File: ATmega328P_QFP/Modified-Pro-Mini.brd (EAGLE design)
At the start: 18.3 x 33.5 mm, 19 parts, among them Q1 8/16/20MHz, U1 ATMEGA328

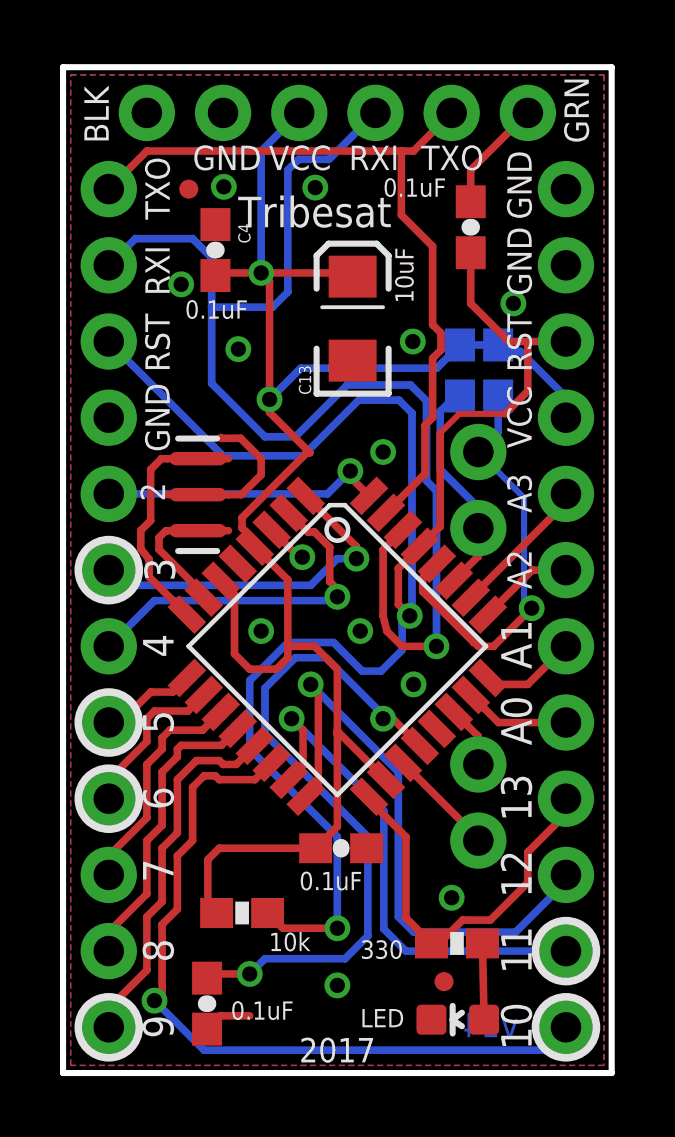
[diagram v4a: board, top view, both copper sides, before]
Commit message: Prepare silkscreen layers for OSH Park printing (#4)
* Fix typo in bPlace layer
* Remove fiducials
* Cleared the tNames layer
* Slight adjustments to prevent text from overlapping copper
* got rid of kink in TXO line
* moved via slightly
* bottom silk tweak
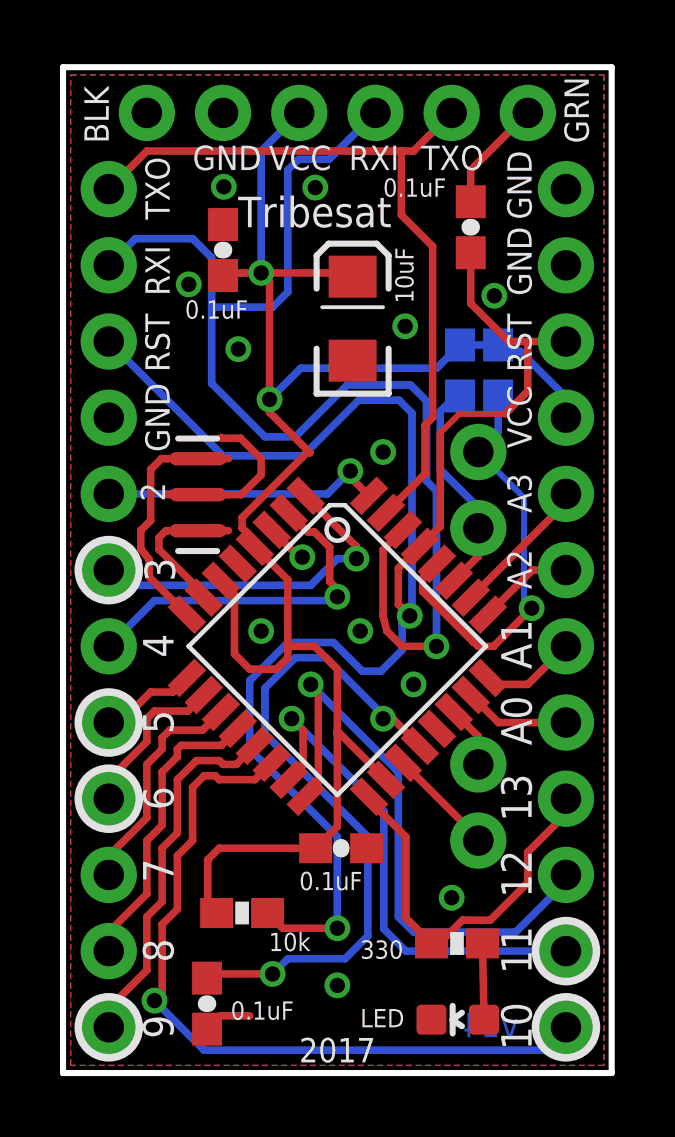
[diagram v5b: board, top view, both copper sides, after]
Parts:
- removed JP5, JP8: FIDUCIALUFIDUCIAL, SparkFun:MICRO-FIDUCIAL
- moved C4 0.25 mm to (5.08, 27.2)
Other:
- board text added: "Test Design V1.0"
- board text removed: "Test Desgine V1.0"
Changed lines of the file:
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@@
 <text x="10.414" y="28.956" size="0.6096" layer="21" font="vector" ratio="13">0.1uF</text>
 <text x="5.334" y="28.702" size="1.016" layer="22" font="vector" ratio="16" rot="MR180">Tribesat</text>
-<text x="14.224" y="24.892" size="0.8128" layer="22" font="vector" ratio="16" rot="MR0">ATmega328P QFP</text>
-<text x="9.398" y="22.86" size="0.8128" layer="22" font="vector" ratio="15" rot="MR0" align="center">Test
-Desgine
-V1.0</text>
 <text x="11.43" y="25.4" size="0.6096" layer="21" font="vector" ratio="13" rot="R90">10uF</text>
 <text x="3.81" y="24.892" size="0.6096" layer="21" font="vector" ratio="13">0.1uF</text>
+<text x="5.588" y="20.828" size="1.016" layer="22" font="vector" ratio="20" distance="10" rot="MR270">ATmega328P QFP</text>
+<text x="8.636" y="23.622" size="0.889" layer="22" font="vector" ratio="20" distance="19" rot="MR0" align="center">Test
+Design
+V1.0</text>
 </plain>
 <attributes>
@@
 <attribute name="VALUE" x="13.1064" y="22.1488" size="0.4064" layer="28" font="vector" rot="MR90"/>
 </element>
-<element name="JP5" library="SparkFun" package="MICRO-FIDUCIAL" value="FIDUCIALUFIDUCIAL" x="3.937" y="29.21"/>
-<element name="JP8" library="SparkFun" package="MICRO-FIDUCIAL" value="FIDUCIALUFIDUCIAL" x="12.446" y="2.794"/>
 <element name="JP3" library="SparkFun" package="1X02" value="" x="13.589" y="7.493" smashed="yes" rot="MR90">
 <attribute name="VALUE" x="10.414" y="6.223" size="1.27" layer="28" rot="MR90"/>
@@
 <attribute name="VALUE" x="14.478" y="26.924" size="0.4064" layer="27" font="vector" rot="R90"/>
 </element>
-<element name="C13" library="SparkFun" package="EIA3216" value="10uF" x="9.398" y="24.892" rot="R90"/>
-<element name="C4" library="SparkFun" package="0603-CAP" value="0.1uF" x="4.826" y="27.178" rot="R270"/>
+<element name="C13" library="SparkFun" package="EIA3216" value="10uF" x="9.398" y="24.892" smashed="yes" rot="R90">
+<attribute name="VALUE" x="8.066" y="25.3" size="0.4064" layer="27" rot="R90"/>
+</element>
+<element name="C4" library="SparkFun" package="0603-CAP" value="0.1uF" x="5.08" y="27.178" smashed="yes" rot="R270">
+<attribute name="VALUE" x="3.937" y="28.194" size="0.4064" layer="27" font="vector" rot="R270"/>
+</element>
 </elements>
 <signals>
@@
 <via x="10.414" y="20.447" extent="1-16" drill="0.508"/>
 <via x="6.35" y="14.478" extent="1-16" drill="0.508"/>
-<via x="14.7574" y="25.4" extent="1-16" drill="0.508"/>
+<via x="14.1224" y="25.654" extent="1-16" drill="0.508"/>
 <via x="7.7216" y="16.9418" extent="1-16" drill="0.508"/>
-<via x="3.683" y="26.035" extent="1-16" drill="0.508"/>
-<via x="11.4046" y="24.13" extent="1-16" drill="0.508"/>
+<via x="3.937" y="26.035" extent="1-16" drill="0.508"/>
+<via x="11.1506" y="24.638" extent="1-16" drill="0.508"/>
 <polygon width="0.254" layer="1" isolate="0.3048">
 <vertex x="0" y="33.02"/>
@@
 <wire x1="10.414" y1="11.557" x2="10.7372" y2="11.557" width="0.254" layer="1"/>
 <via x="10.414" y="11.557" extent="1-16" drill="0.508"/>
-<wire x1="9.144" y1="3.556" x2="6.477" y2="3.556" width="0.254" layer="16"/>
-<wire x1="6.477" y1="3.556" x2="5.969" y2="3.048" width="0.254" layer="16"/>
-<via x="5.969" y="3.048" extent="1-16" drill="0.508"/>
-<wire x1="5.969" y1="3.048" x2="4.6872" y2="3.048" width="0.254" layer="1"/>
+<wire x1="9.144" y1="3.556" x2="7.239" y2="3.556" width="0.254" layer="16"/>
+<wire x1="7.239" y1="3.556" x2="6.731" y2="3.048" width="0.254" layer="16"/>
+<via x="6.731" y="3.048" extent="1-16" drill="0.508"/>
+<wire x1="6.731" y1="3.048" x2="4.6872" y2="3.048" width="0.254" layer="1"/>
 <wire x1="4.6872" y1="3.048" x2="4.5466" y2="2.9074" width="0.254" layer="1"/>
 <wire x1="11.64248125" y1="10.651828125" x2="10.737309375" y2="11.557" width="0.254" layer="1"/>
@@
 <contactref element="JP1" pad="2"/>
 <wire x1="2.54" y1="30.48" x2="1.27" y2="29.21" width="0.254" layer="1"/>
-<wire x1="11.43" y1="30.48" x2="11.049" y2="30.48" width="0.254" layer="1"/>
+<wire x1="11.43" y1="30.48" x2="11.0236" y2="30.48" width="0.254" layer="1"/>
 <wire x1="11.0236" y1="30.48" x2="2.54" y2="30.48" width="0.254" layer="1"/>
 <wire x1="11.43" y1="30.48" x2="12.7" y2="31.75" width="0.254" layer="1"/>
-<wire x1="12.065" y1="21.59" x2="12.065" y2="23.5712" width="0.254" layer="1"/>
-<wire x1="12.065" y1="23.5712" x2="12.3444" y2="23.8506" width="0.254" layer="1"/>
-<wire x1="12.3444" y1="23.8506" x2="12.3444" y2="24.4094" width="0.254" layer="1"/>
-<wire x1="12.3444" y1="24.4094" x2="12.065" y2="24.6888" width="0.254" layer="1"/>
-<wire x1="12.065" y1="24.6888" x2="12.065" y2="27.305" width="0.254" layer="1"/>
-<wire x1="11.811" y1="21.336" x2="12.065" y2="21.59" width="0.254" layer="1"/>
+<wire x1="12.065" y1="21.59" x2="11.811" y2="21.336" width="0.254" layer="1"/>
 <wire x1="11.811" y1="19.7194" x2="11.811" y2="21.336" width="0.254" layer="1"/>
 <wire x1="10.5111125" y1="18.4195375" x2="11.810975" y2="19.7194" width="0.254" layer="1"/>
 <wire x1="11.810975" y1="19.7194" x2="11.811" y2="19.7194" width="0.254" layer="1"/>
-<wire x1="12.065" y1="27.305" x2="11.0236" y2="28.3464" width="0.254" layer="1"/>
+<wire x1="11.0236" y1="28.3464" x2="12.065" y2="27.305" width="0.254" layer="1"/>
 <wire x1="11.0236" y1="28.3464" x2="11.0236" y2="30.48" width="0.254" layer="1"/>
-<wire x1="11.0236" y1="30.48" x2="11.049" y2="30.48" width="0.254" layer="1"/>
+<wire x1="12.065" y1="27.305" x2="12.065" y2="21.59" width="0.254" layer="1"/>
 </signal>
 <signal name="VCC">
@@
 <contactref element="C13" pad="A"/>
 <contactref element="C4" pad="2"/>
-<wire x1="6.35" y1="26.416" x2="4.914" y2="26.416" width="0.254" layer="1"/>
-<wire x1="4.914" y1="26.416" x2="4.826" y2="26.328" width="0.254" layer="1"/>
+<wire x1="6.35" y1="26.416" x2="5.676" y2="26.416" width="0.254" layer="1"/>
+<wire x1="5.676" y1="26.416" x2="5.08" y2="26.328" width="0.254" layer="1"/>
 <wire x1="6.35" y1="26.416" x2="9.274" y2="26.416" width="0.254" layer="1"/>
 <wire x1="9.274" y1="26.416" x2="9.398" y2="26.292" width="0.254" layer="1"/>

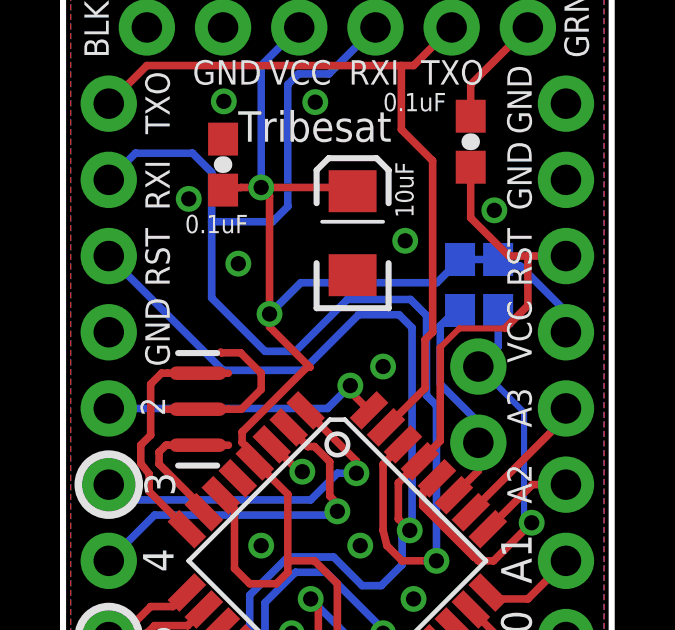
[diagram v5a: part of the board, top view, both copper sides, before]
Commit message: straigtened VCC line
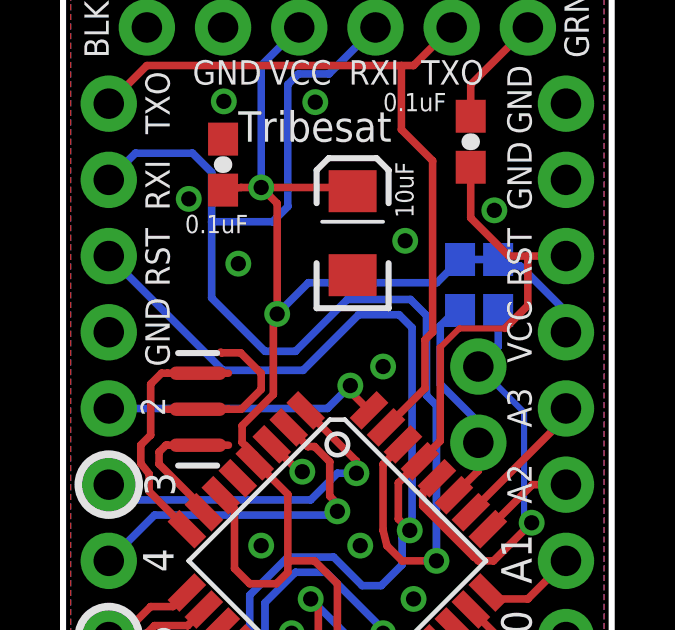
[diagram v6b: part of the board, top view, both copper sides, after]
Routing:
- net VCC: track 58.8 -> 57.7 mm
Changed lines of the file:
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@@
 <wire x1="16.51" y1="22.2758" x2="16.51" y2="21.59" width="0.254" layer="16"/>
 <wire x1="14.986" y1="23.7998" x2="16.51" y2="22.2758" width="0.254" layer="16"/>
-<wire x1="7.6708" y1="23.241" x2="12.2056" y2="23.241" width="0.254" layer="16"/>
 <wire x1="12.9794" y1="24.0148" x2="14.2494" y2="24.0148" width="0.254" layer="16"/>
-<via x="6.6294" y="22.1996" extent="1-16" drill="0.508"/>
+<via x="6.8834" y="22.1996" extent="1-16" drill="0.508"/>
 <wire x1="8.89" y1="11.0491" x2="8.89" y2="7.962" width="0.254" layer="1"/>
 <wire x1="8.89" y1="7.962" x2="8.167" y2="7.239" width="0.254" layer="1"/>
@@
 <wire x1="6.137515625" y1="17.28816875" x2="7.239" y2="16.186684375" width="0.254" layer="1"/>
 <wire x1="10.5111125" y1="9.520459375" x2="8.89" y2="11.141571875" width="0.254" layer="1"/>
-<wire x1="12.2056" y1="23.241" x2="12.9794" y2="24.0148" width="0.254" layer="16"/>
+<wire x1="12.9794" y1="24.0148" x2="12.2056" y2="23.241" width="0.254" layer="16"/>
 <wire x1="14.986" y1="23.7998" x2="14.4644" y2="23.7998" width="0.254" layer="16"/>
 <wire x1="14.4644" y1="23.7998" x2="14.2494" y2="24.0148" width="0.254" layer="16"/>
@@
 <wire x1="7.62" y1="31.75" x2="6.35" y2="30.48" width="0.254" layer="16"/>
 <wire x1="6.137515625" y1="17.313484375" x2="6.137515625" y2="17.28816875" width="0.254" layer="1"/>
-<wire x1="5.715" y1="17.9138" x2="5.715" y2="18.2626" width="0.254" layer="1"/>
-<wire x1="5.715" y1="18.2626" x2="7.874" y2="20.4216" width="0.254" layer="1"/>
 <wire x1="6.137515625" y1="17.491284375" x2="5.715" y2="17.9138" width="0.254" layer="1"/>
 <wire x1="6.137515625" y1="17.491284375" x2="6.137515625" y2="17.28816875" width="0.254" layer="1"/>
-<wire x1="7.9756" y1="20.4216" x2="6.6294" y2="21.7678" width="0.254" layer="1"/>
-<wire x1="7.6708" y1="23.241" x2="6.6294" y2="22.1996" width="0.254" layer="16"/>
-<wire x1="6.6294" y1="21.7678" x2="6.6294" y2="22.1996" width="0.254" layer="1"/>
-<wire x1="6.6294" y1="22.1996" x2="6.6294" y2="22.5044" width="0.254" layer="1"/>
 <contactref element="R2" pad="2"/>
 <wire x1="4.572" y1="6.858" x2="4.572" y2="5.373" width="0.254" layer="1"/>
 <wire x1="4.572" y1="5.373" x2="4.865" y2="5.08" width="0.254" layer="1"/>
-<wire x1="7.874" y1="20.4216" x2="7.9756" y2="20.4216" width="0.254" layer="1"/>
-<wire x1="6.6294" y1="22.1996" x2="6.6294" y2="26.1366" width="0.254" layer="1"/>
-<wire x1="6.6294" y1="26.1366" x2="6.35" y2="26.416" width="0.254" layer="1"/>
+<wire x1="6.35" y1="26.416" x2="6.6294" y2="26.1366" width="0.254" layer="1"/>
 <contactref element="C13" pad="A"/>
 <contactref element="C4" pad="2"/>
@@
 <wire x1="6.35" y1="26.416" x2="9.274" y2="26.416" width="0.254" layer="1"/>
 <wire x1="9.274" y1="26.416" x2="9.398" y2="26.292" width="0.254" layer="1"/>
+<wire x1="6.7564" y1="22.0726" x2="6.8834" y2="22.1996" width="0.254" layer="1"/>
+<wire x1="5.715" y1="18.4752625" x2="6.7564" y2="19.5166625" width="0.254" layer="1"/>
+<wire x1="6.7564" y1="19.5166625" x2="6.7564" y2="22.0726" width="0.254" layer="1"/>
+<wire x1="5.715" y1="17.9138" x2="5.715" y2="18.4752625" width="0.254" layer="1"/>
+<wire x1="6.8834" y1="22.1996" x2="6.8834" y2="25.8826" width="0.254" layer="1"/>
+<wire x1="6.8834" y1="25.8826" x2="6.35" y2="26.416" width="0.254" layer="1"/>
+<wire x1="12.2056" y1="23.241" x2="7.9248" y2="23.241" width="0.254" layer="16"/>
+<wire x1="7.9248" y1="23.241" x2="6.8834" y2="22.1996" width="0.254" layer="16"/>
 </signal>
 <signal name="D9">

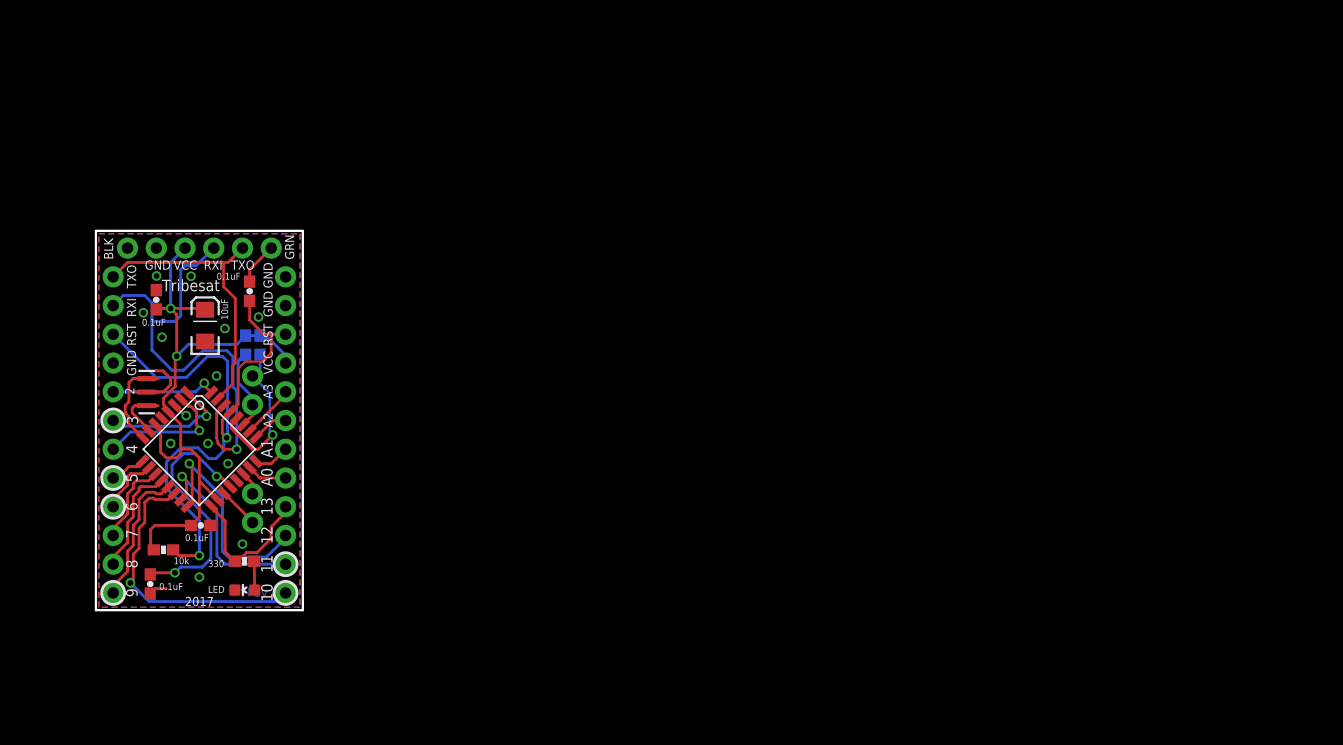
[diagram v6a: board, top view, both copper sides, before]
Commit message: New board design: - larger footprint by the ICD requirements (no holes) - removed headers - added DF12 connector footprint
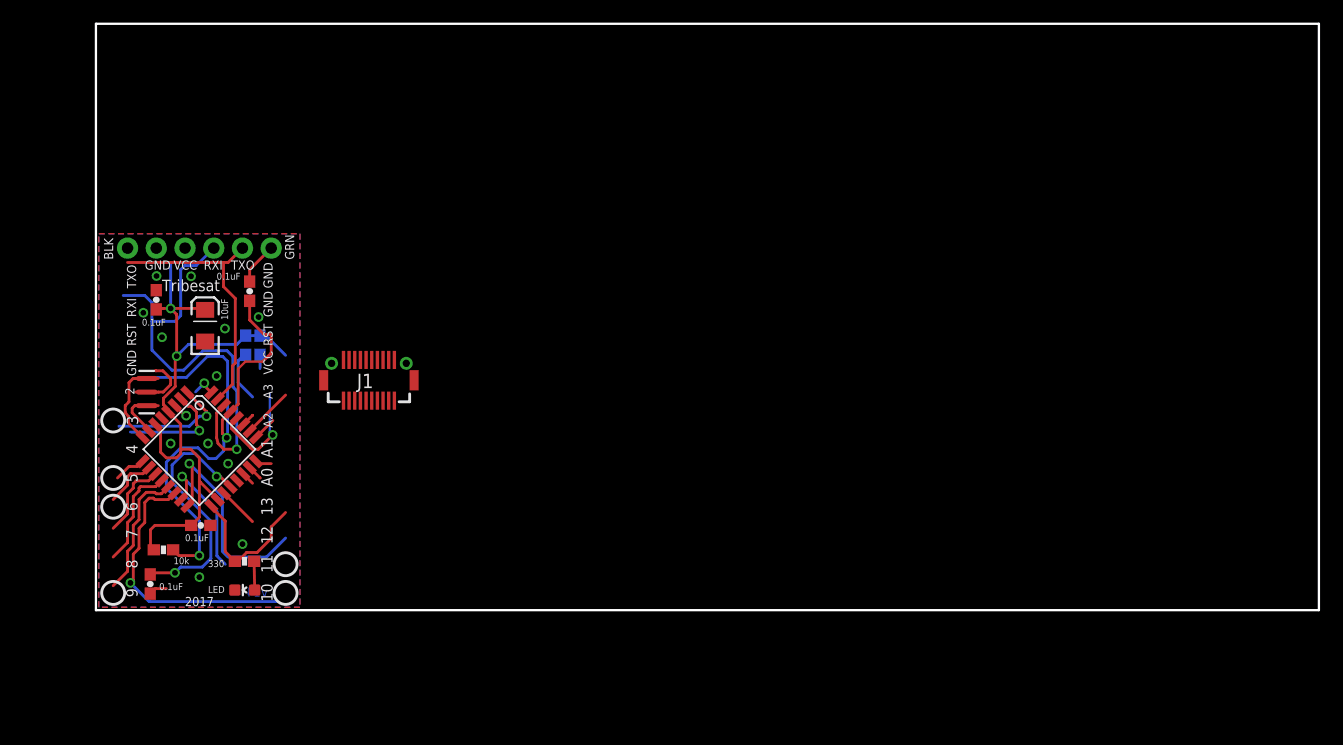
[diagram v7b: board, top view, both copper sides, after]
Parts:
- removed JP2, JP3: (no value), SparkFun:1X02
- removed JP6, JP7: (no value), SparkFun:1X12
- added J1: DF12(4.0)-20DP-0.5V(86), DF12(4.0)-20DP-0.5V(86):DF12(4.0)-20DP
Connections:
- new net 1W: J1.16
- new net 3.3V: J1.18
- new net BUSY: J1.13
- new net D1: J1.7
- new net LVRX: J1.9
- new net LVTX: J1.10
- new net N$9: J1.15
- new net NC: J1.14
- net A0: no longer JP6.8
- net A1: now also J1.1; no longer JP6.7
- net A2: now also J1.2; no longer JP6.6
- net A3: now also J1.3; no longer JP6.5
- net A4: now also J1.4; no longer JP2.1
- net A5: now also J1.5; no longer JP2.2
- net A6: now also J1.6; no longer JP3.1
- net A7: no longer JP3.2
- net D10: no longer JP6.12
- net D2: now also J1.8; no longer JP7.8
- net D3: no longer JP7.7
- net D4: no longer JP7.6
- net D5: no longer JP7.5
- net D6: no longer JP7.4
- net D7: no longer JP7.3
- net D8: no longer JP7.2
- net D9: no longer JP7.1
- net GND: now also J1.19, J1.20; no longer JP1.5, JP1.6, JP6.1, JP6.2, JP7.9
- net MISO: no longer JP6.10
- net MOSI: no longer JP6.11
- net RESET: no longer JP6.3, JP7.10
- net RXI: now also J1.12; no longer JP7.11
- net SCK: no longer JP6.9
- net TXO: now also J1.11; no longer JP7.12
- net VCC: now also J1.17; no longer JP1.4, JP6.4
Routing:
- net D2: track 9.45 -> 2.16 mm
- net RESET: track 56.3 -> 49.7 mm
- net MOSI: track 17.1 -> 11.7 mm
- net A5: track 14.1 -> 11.0 mm
- net VCC: track 57.7 -> 55.2 mm
- net A0: track 3.55 -> 1.30 mm
- net D4: track 12.3 -> 10.1 mm
- net TXO: track 25.6 -> 23.8 mm
- net A1: track 3.31 -> 1.51 mm
- net A4: track 7.67 -> 6.04 mm
- net RXI: track 41.5 -> 40.2 mm
- net A2: track 3.22 -> 2.10 mm
- net D10: track 25.4 -> 24.4 mm
- net A7: track 2.09 -> 1.15 mm
- net D6: track 5.71 -> 4.79 mm
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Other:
- board size 18.3 x 33.5 mm -> 108.1 x 51.8 mm
